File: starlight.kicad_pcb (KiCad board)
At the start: 2 copper layers, 210 x 210 mm, 72 parts, among them J1 Conn_01x06, U1 AT42QT1012-T, U2 TPS923610DRLR

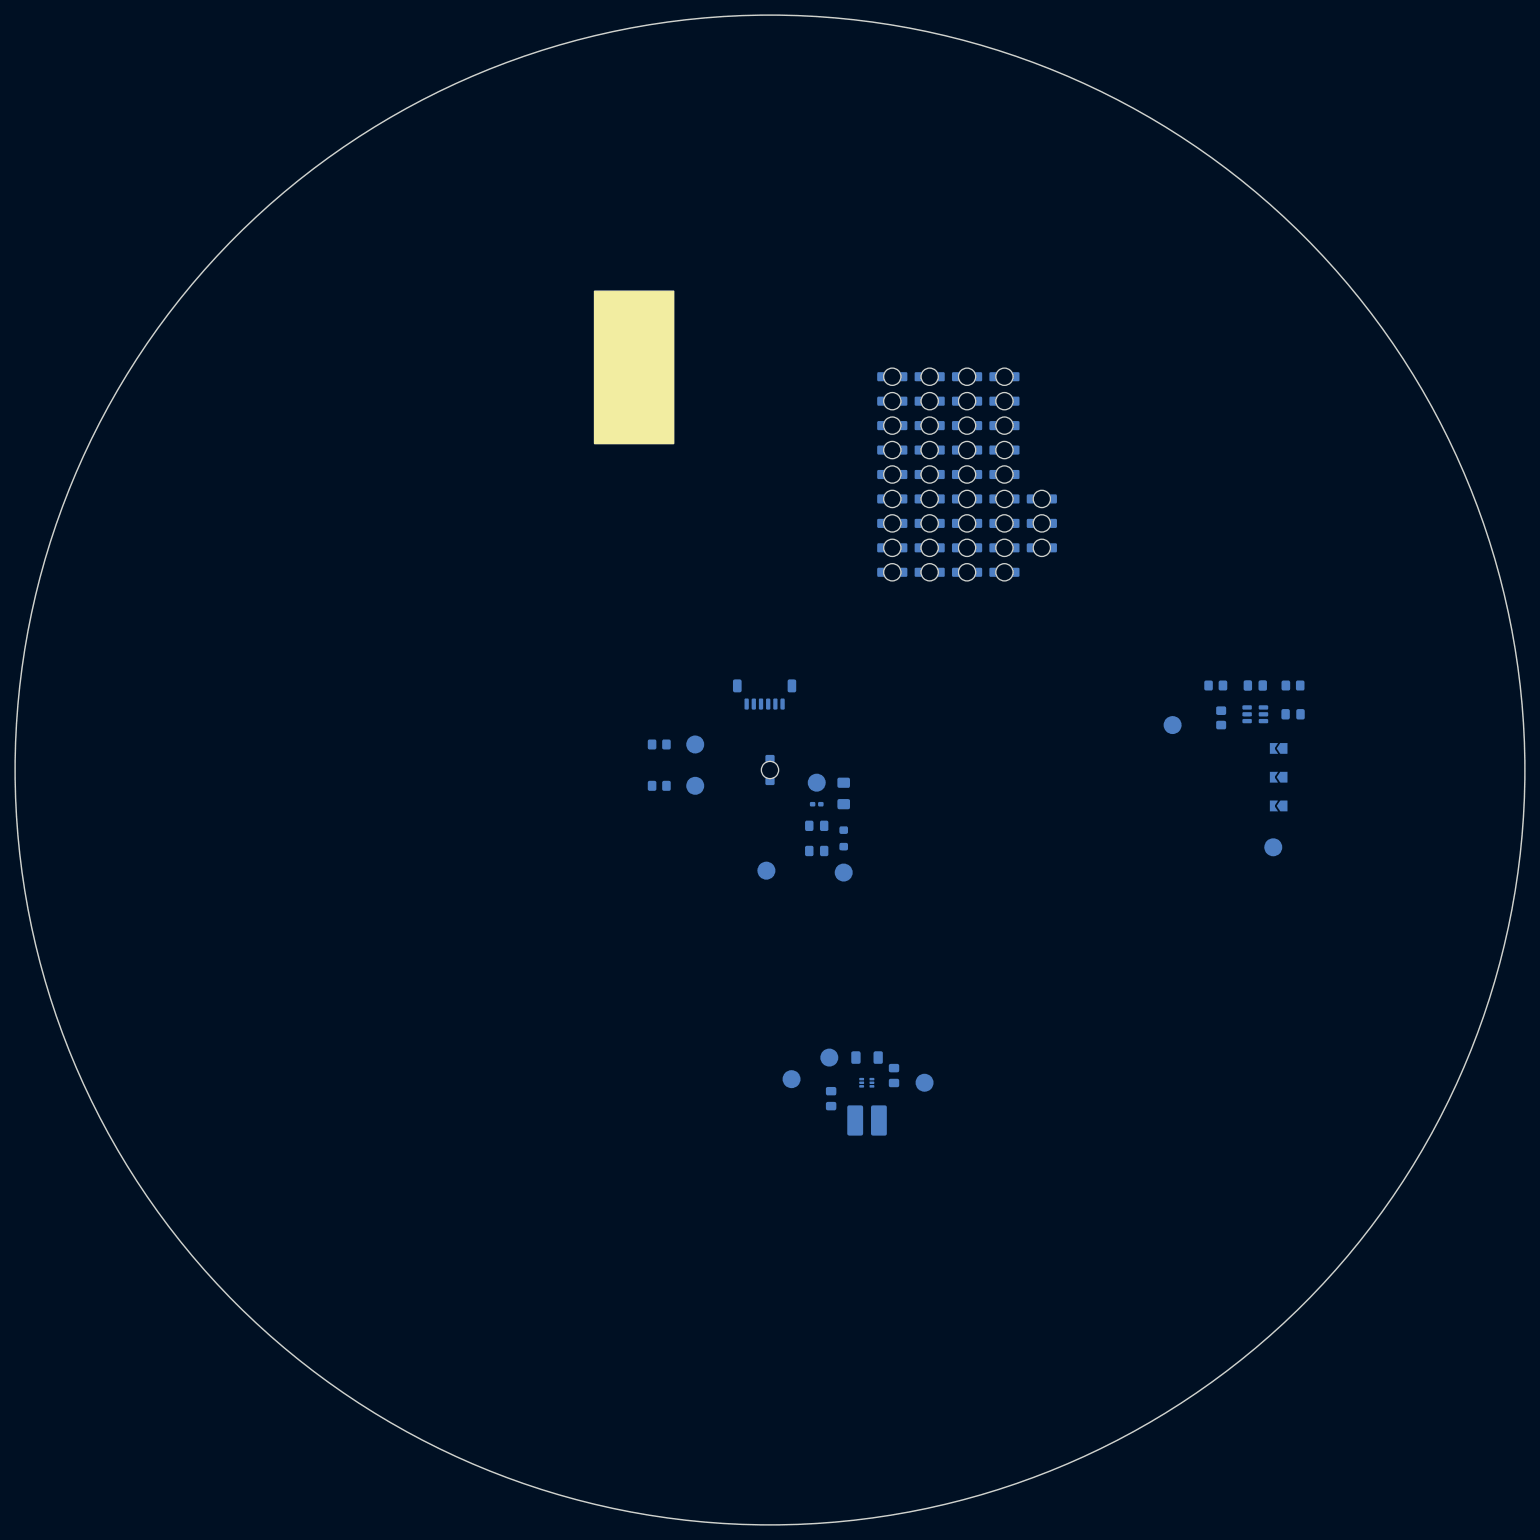
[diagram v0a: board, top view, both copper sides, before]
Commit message: Placed all LEDs at stars' locations using a Python script.
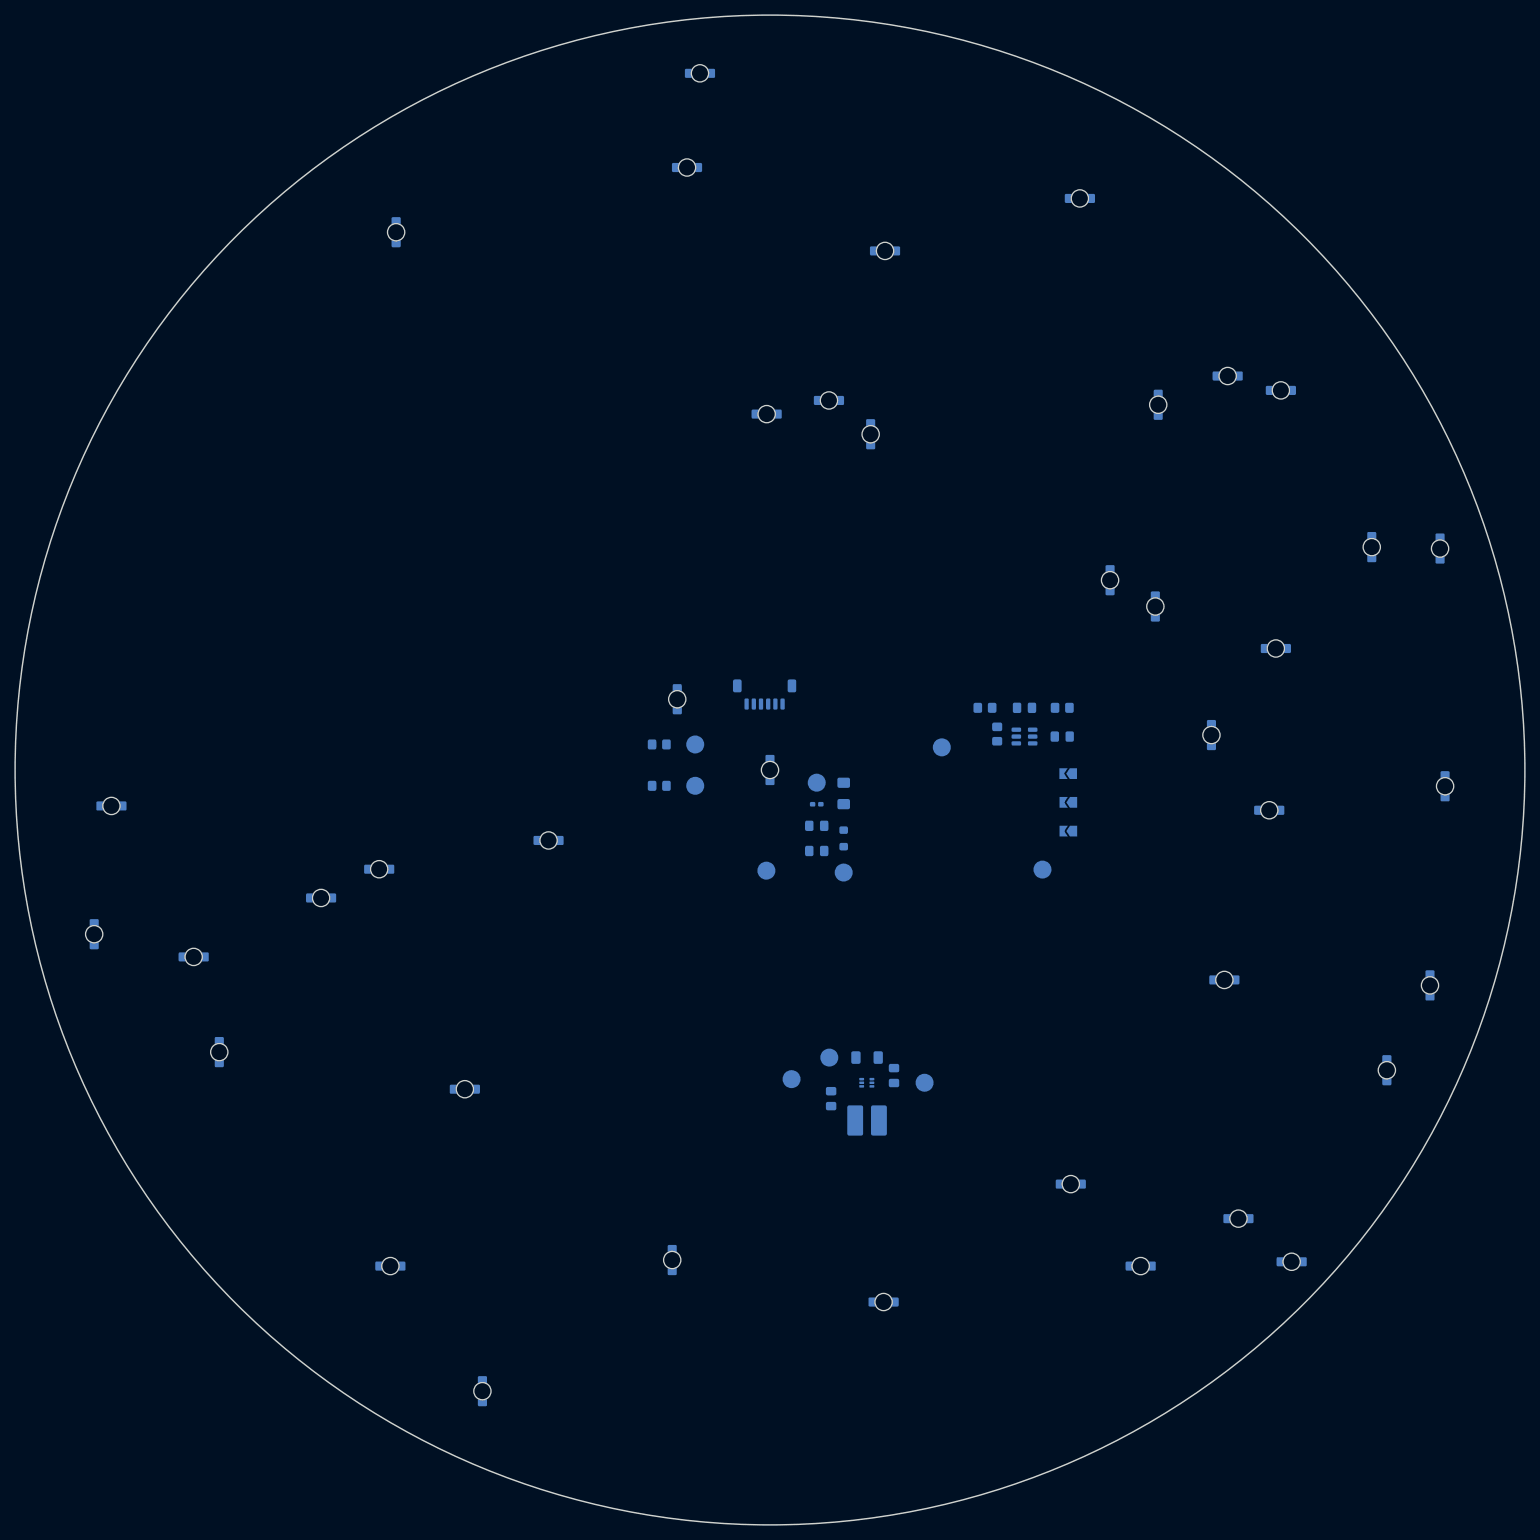
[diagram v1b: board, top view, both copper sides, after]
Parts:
- moved D7 142.8 mm to (105.5, 286.4), turned to 90 degrees
- moved D18 137.8 mm to (51.5, 222.8), turned to -90 degrees
- moved D10 132.6 mm to (68.9, 239.2), turned to -90 degrees
- moved D6 130.4 mm to (92.7, 269.0)
- moved D27 127.9 mm to (218.1, 268.4), turned to 180 degrees
- moved D19 127.1 mm to (197.1, 269.0), turned to 180 degrees
- moved D22 125.3 mm to (53.9, 205.0), turned to 180 degrees
- moved D14 120.6 mm to (65.3, 226.0)
- moved D26 111.3 mm to (83.1, 217.8), turned to 180 degrees
- moved D23 107.0 mm to (210.7, 262.4), turned to 180 degrees
- moved D3 103.7 mm to (131.9, 268.2), turned to 90 degrees
- moved D11 101.7 mm to (161.3, 274.0), turned to 180 degrees
- moved D15 100.6 mm to (187.3, 257.6), turned to 180 degrees
- moved D35 97.8 mm to (237.3, 230.0), turned to -90 degrees
- moved D30 97.8 mm to (91.1, 213.8), turned to 180 degrees
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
